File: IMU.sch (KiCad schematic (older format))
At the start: 0 parts

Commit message: Added IMU module
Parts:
- added C?: 100nF, Capacitors_SMD:C_0603, symbol C
- added R802, R803, R804, R805, R806, R807, R?: 10K, Resistors_SMD:R_0603, symbol R
- added U?: IMU, Housings_LGA:Bosch_LGA-14_3x2.5mm_Pitch0.5mm, symbol IMU
- added U?: Level_Shifter_4Channel, symbol Level_Shifter_4Channel
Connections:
- new net: R?.1, U?.1 (SDO/SA0), U?.12 (CS)
- new net +1V8: C?.1, R802.2, R803.2, R?.2, U?.1 (Vref_A), U?.5 (VDDIO), U?.8 (VDD)
- new net +5V: R806.2, R807.2, U?.14 (Vref_B), U?.8 (EN)
- new net GND: C?.2, R804.2, R805.2, U?.2 (SDx), U?.3 (SCx), U?.6 (GND), U?.7 (GND), U?.7 (GND)
- new net INT1: R804.1, U?.10 (B4)
- new net INT1_1V8: U?.4 (INT1), U?.5 (A4)
- new net INT2: R805.1, U?.11 (B3)
- new net INT2_1V8: U?.4 (A3), U?.9 (INT2)
- new net SCL: R807.1, U?.13 (B1)
- new net SCL_1V8: R802.1, U?.13 (SCL), U?.3 (A2)
- new net SDA: R806.1, U?.12 (B2)
- new net SDA_1V8: R803.1, U?.14 (SDA), U?.2 (A1)
- no-connect marks 0 -> 2

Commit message: Finished Schematic
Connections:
- net +5V renamed +3V3
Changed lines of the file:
@@
 NoConn ~ 3375 3825
-$Comp
-L +5V #PWR0120
-U 1 1 5A13EF18
-P 7800 3250
-F 0 "#PWR0120" H 7800 3100 50  0001 C CNN
-F 1 "+5V" H 7800 3390 50  0000 C CNN
-F 2 "" H 7800 3250 50  0001 C CNN
-F 3 "" H 7800 3250 50  0001 C CNN
-	1    7800 3250
-	1    0    0    -1
-$EndComp
 $Comp
 L R R805
@@
 Wire Wire Line
 	7625 4250 7625 4450
-$Comp
-L +5V #PWR0121
-U 1 1 5A13EF46
-P 8575 4850
-F 0 "#PWR0121" H 8575 4700 50  0001 C CNN
-F 1 "+5V" H 8575 4990 50  0000 C CNN
-F 2 "" H 8575 4850 50  0001 C CNN
-F 3 "" H 8575 4850 50  0001 C CNN
-	1    8575 4850
-	1    0    0    -1
-$EndComp
 Wire Wire Line
 	7625 4750 7625 4850
@@
 	1    0    0    -1
 $EndComp
+$Comp
+L +3V3 #PWR?
+U 1 1 5AC02D08
+P 7800 3250
+F 0 "#PWR?" H 7800 3100 50  0001 C CNN
+F 1 "+3V3" H 7800 3390 50  0000 C CNN
+F 2 "" H 7800 3250 50  0001 C CNN
+F 3 "" H 7800 3250 50  0001 C CNN
+	1    7800 3250
+	1    0    0    -1
+$EndComp
+$Comp
+L +3V3 #PWR?
+U 1 1 5AC02D38
+P 8575 4850
+F 0 "#PWR?" H 8575 4700 50  0001 C CNN
+F 1 "+3V3" H 8575 4990 50  0000 C CNN
+F 2 "" H 8575 4850 50  0001 C CNN
+F 3 "" H 8575 4850 50  0001 C CNN
+	1    8575 4850
+	1    0    0    -1
+$EndComp

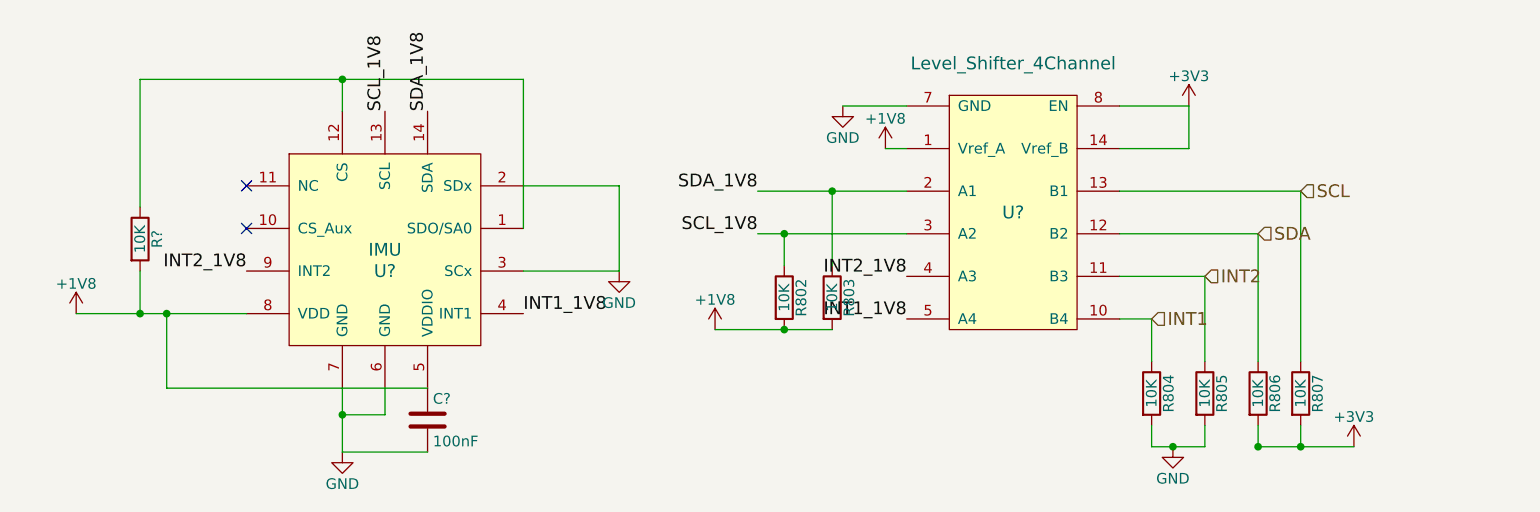
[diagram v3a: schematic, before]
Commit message: Started associating footprints
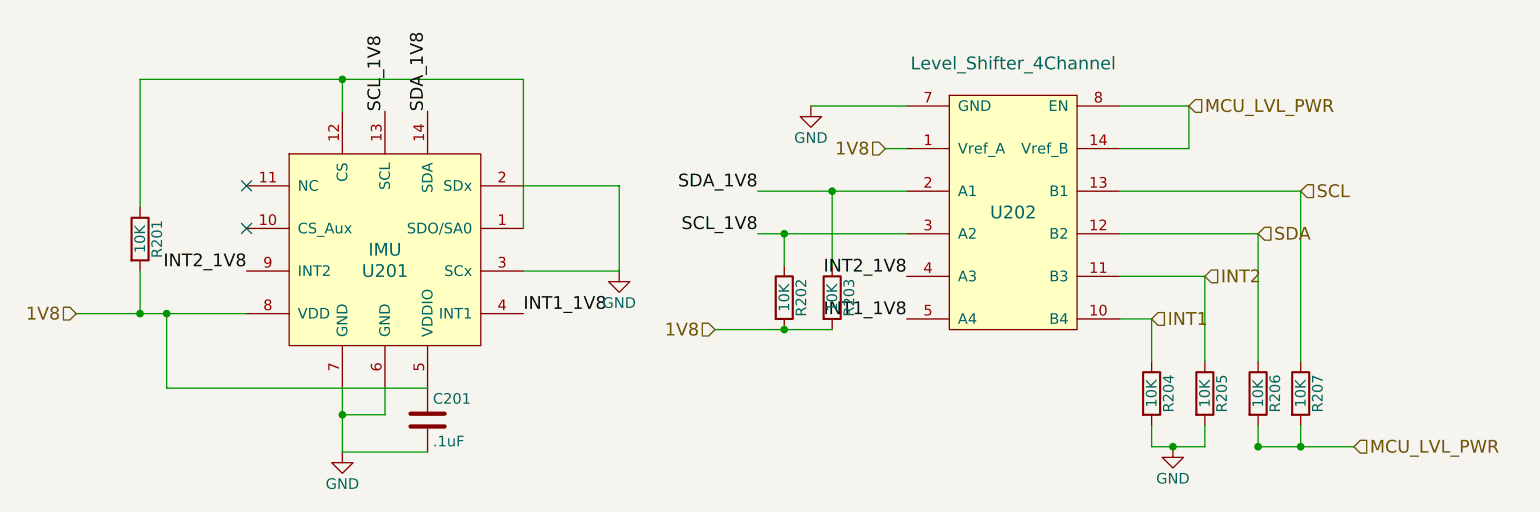
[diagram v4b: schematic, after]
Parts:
- C201: renamed from C?; value 100nF -> .1uF; footprint Capacitors_SMD:C_0603 -> Capacitors_SMD:C_0402
- gave numbers to parts that had none: 3
- renumbered R802 to R202, R803 to R203, R804 to R204, R805 to R205, R806 to R206, R807 to R207
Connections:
- net +1V8 renamed 1V8
- net +3V3 renamed MCU_LVL_PWR
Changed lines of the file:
@@
 $EndDescr
 $Comp
-L IMU U?
+L IMU U201
 U 1 1 5A13EED2
 P 4025 3925
-F 0 "U?" H 4025 3825 60  0000 C CNN
+F 0 "U201" H 4025 3825 60  0000 C CNN
 F 1 "IMU" H 4025 3925 60  0000 C CNN
 F 2 "Housings_LGA:Bosch_LGA-14_3x2.5mm_Pitch0.5mm" H 4025 3925 60  0001 C CNN
@@
 $EndComp
 $Comp
-L R R?
+L R R201
 U 1 1 5A13EED9
 P 2875 3875
-F 0 "R?" V 2955 3875 50  0000 C CNN
+F 0 "R201" V 2955 3875 50  0000 C CNN
 F 1 "10K" V 2875 3875 50  0000 C CNN
 F 2 "Resistors_SMD:R_0603" V 2805 3875 50  0001 C CNN
@@
 $EndComp
 $Comp
-L C C?
+L C C201
 U 1 1 5A13EEE0
 P 4225 4725
-F 0 "C?" H 4250 4825 50  0000 L CNN
-F 1 "100nF" H 4250 4625 50  0000 L CNN
-F 2 "Capacitors_SMD:C_0603" H 4263 4575 50  0001 C CNN
+F 0 "C201" H 4250 4825 50  0000 L CNN
+F 1 ".1uF" H 4250 4625 50  0000 L CNN
+F 2 "Capacitors_SMD:C_0402" H 4263 4575 50  0001 C CNN
 F 3 "" H 4225 4725 50  0001 C CNN
 	1    4225 4725
@@
 $EndComp
 $Comp
-L GND #PWR0117
+L GND #PWR09
 U 1 1 5A13EEE7
 P 3825 4875
-F 0 "#PWR0117" H 3825 4625 50  0001 C CNN
+F 0 "#PWR09" H 3825 4625 50  0001 C CNN
 F 1 "GND" H 3825 4725 50  0000 C CNN
 F 2 "" H 3825 4875 50  0001 C CNN
@@
 $EndComp
 $Comp
-L GND #PWR0118
+L GND #PWR010
 U 1 1 5A13EEED
 P 5125 4025
-F 0 "#PWR0118" H 5125 3775 50  0001 C CNN
+F 0 "#PWR010" H 5125 3775 50  0001 C CNN
 F 1 "GND" H 5125 3875 50  0000 C CNN
 F 2 "" H 5125 4025 50  0001 C CNN
 F 3 "" H 5125 4025 50  0001 C CNN
 	1    5125 4025
-	1    0    0    -1
-$EndComp
-$Comp
-L +1V8 #PWR0119
-U 1 1 5A13EEF3
-P 2575 4225
-F 0 "#PWR0119" H 2575 4075 50  0001 C CNN
-F 1 "+1V8" H 2575 4365 50  0000 C CNN
-F 2 "" H 2575 4225 50  0001 C CNN
-F 3 "" H 2575 4225 50  0001 C CNN
-	1    2575 4225
 	1    0    0    -1
 $EndComp
@@
 NoConn ~ 3375 3825
 $Comp
-L R R805
+L R R205
 U 1 1 5A13EF1E
 P 7875 4600
-F 0 "R805" V 7955 4600 50  0000 C CNN
+F 0 "R205" V 7955 4600 50  0000 C CNN
 F 1 "10K" V 7875 4600 50  0000 C CNN
 F 2 "Resistors_SMD:R_0603" V 7805 4600 50  0001 C CNN
@@
 $EndComp
 $Comp
-L R R804
+L R R204
 U 1 1 5A13EF25
 P 7625 4600
-F 0 "R804" V 7705 4600 50  0000 C CNN
+F 0 "R204" V 7705 4600 50  0000 C CNN
 F 1 "10K" V 7625 4600 50  0000 C CNN
 F 2 "Resistors_SMD:R_0603" V 7555 4600 50  0001 C CNN
@@
 $EndComp
 $Comp
-L R R806
+L R R206
 U 1 1 5A13EF2C
 P 8125 4600
-F 0 "R806" V 8205 4600 50  0000 C CNN
+F 0 "R206" V 8205 4600 50  0000 C CNN
 F 1 "10K" V 8125 4600 50  0000 C CNN
 F 2 "Resistors_SMD:R_0603" V 8055 4600 50  0001 C CNN
@@
 $EndComp
 $Comp
-L R R807
+L R R207
 U 1 1 5A13EF33
 P 8325 4600
-F 0 "R807" V 8405 4600 50  0000 C CNN
+F 0 "R207" V 8405 4600 50  0000 C CNN
 F 1 "10K" V 8325 4600 50  0000 C CNN
 F 2 "Resistors_SMD:R_0603" V 8255 4600 50  0001 C CNN
@@
 	7800 3450 7800 3250
 $Comp
-L GND #PWR0122
+L GND #PWR011
 U 1 1 5A13EF57
-P 6175 3250
-F 0 "#PWR0122" H 6175 3000 50  0001 C CNN
-F 1 "GND" H 6175 3100 50  0000 C CNN
-F 2 "" H 6175 3250 50  0001 C CNN
-F 3 "" H 6175 3250 50  0001 C CNN
-	1    6175 3250
-	1    0    0    -1
-$EndComp
-Wire Wire Line
-	6475 3250 6175 3250
-$Comp
-L +1V8 #PWR0123
-U 1 1 5A13EF5E
-P 6375 3450
-F 0 "#PWR0123" H 6375 3300 50  0001 C CNN
-F 1 "+1V8" H 6375 3590 50  0000 C CNN
-F 2 "" H 6375 3450 50  0001 C CNN
-F 3 "" H 6375 3450 50  0001 C CNN
-	1    6375 3450
+P 6025 3250
+F 0 "#PWR011" H 6025 3000 50  0001 C CNN
+F 1 "GND" H 6025 3100 50  0000 C CNN
+F 2 "" H 6025 3250 50  0001 C CNN
+F 3 "" H 6025 3250 50  0001 C CNN
+	1    6025 3250
 	1    0    0    -1
 $EndComp
@@
 SCL_1V8
 $Comp
-L R R803
+L R R203
 U 1 1 5A13EF67
 P 6125 4150
-F 0 "R803" V 6205 4150 50  0000 C CNN
+F 0 "R203" V 6205 4150 50  0000 C CNN
 F 1 "10K" V 6125 4150 50  0000 C CNN
 F 2 "Resistors_SMD:R_0603" V 6055 4150 50  0001 C CNN
@@
 $EndComp
 $Comp
-L R R802
+L R R202
 U 1 1 5A13EF6E
 P 5900 4150
-F 0 "R802" V 5980 4150 50  0000 C CNN
+F 0 "R202" V 5980 4150 50  0000 C CNN
 F 1 "10K" V 5900 4150 50  0000 C CNN
 F 2 "Resistors_SMD:R_0603" V 5830 4150 50  0001 C CNN
@@
 	5900 3850 5900 4000
 Connection ~ 5900 3850
-$Comp
-L +1V8 #PWR0124
-U 1 1 5A13EF7D
-P 5575 4300
-F 0 "#PWR0124" H 5575 4150 50  0001 C CNN
-F 1 "+1V8" H 5575 4440 50  0000 C CNN
-F 2 "" H 5575 4300 50  0001 C CNN
-F 3 "" H 5575 4300 50  0001 C CNN
-	1    5575 4300
-	1    0    0    -1
-$EndComp
 Wire Wire Line
 	5575 4300 6125 4300
@@
 INT2
 $Comp
-L GND #PWR0125
+L GND #PWR012
 U 1 1 5A04C7D6
 P 7725 4850
-F 0 "#PWR0125" H 7725 4600 50  0001 C CNN
+F 0 "#PWR012" H 7725 4600 50  0001 C CNN
 F 1 "GND" H 7725 4700 50  0000 C CNN
 F 2 "" H 7725 4850 50  0001 C CNN
@@
 Connection ~ 3825 3125
 $Comp
-L Level_Shifter_4Channel U?
+L Level_Shifter_4Channel U202
 U 1 1 5AA8177A
 P 6975 3750
-F 0 "U?" H 6975 3750 60  0000 C CNN
+F 0 "U202" H 6975 3750 60  0000 C CNN
 F 1 "Level_Shifter_4Channel" H 6975 4450 60  0000 C CNN
 F 2 "" H 6975 3750 60  0001 C CNN
@@
 	1    0    0    -1
 $EndComp
-$Comp
-L +3V3 #PWR?
-U 1 1 5AC02D08
-P 7800 3250
-F 0 "#PWR?" H 7800 3100 50  0001 C CNN
-F 1 "+3V3" H 7800 3390 50  0000 C CNN
-F 2 "" H 7800 3250 50  0001 C CNN
-F 3 "" H 7800 3250 50  0001 C CNN
-	1    7800 3250
-	1    0    0    -1
-$EndComp
-$Comp
-L +3V3 #PWR?
-U 1 1 5AC02D38
-P 8575 4850
-F 0 "#PWR?" H 8575 4700 50  0001 C CNN
-F 1 "+3V3" H 8575 4990 50  0000 C CNN
-F 2 "" H 8575 4850 50  0001 C CNN
-F 3 "" H 8575 4850 50  0001 C CNN
-	1    8575 4850
-	1    0    0    -1
-$EndComp
+Text HLabel 8575 4850 2    60   Input ~ 0
+MCU_LVL_PWR
+Text HLabel 6375 3450 0    60   Input ~ 0
+1V8
+Wire Wire Line
+	6475 3250 6025 3250
+Text HLabel 2575 4225 0    60   Input ~ 0
+1V8
+Text HLabel 7800 3250 2    60   Input ~ 0
+MCU_LVL_PWR
+Text HLabel 5575 4300 0    60   Input ~ 0
+1V8
 $EndSCHEMATC
